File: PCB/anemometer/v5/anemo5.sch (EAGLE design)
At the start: 64 parts, among them IC1 AD8223, IC2 AD8223, IC3 AD8223, IC4 AD8223, IC6 TL072D, J1 RJ12STRAIGHT-I2C, J2 RJ12STRAIGHT-I2C, T1 BC846, T2 BC846, T3 BC846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

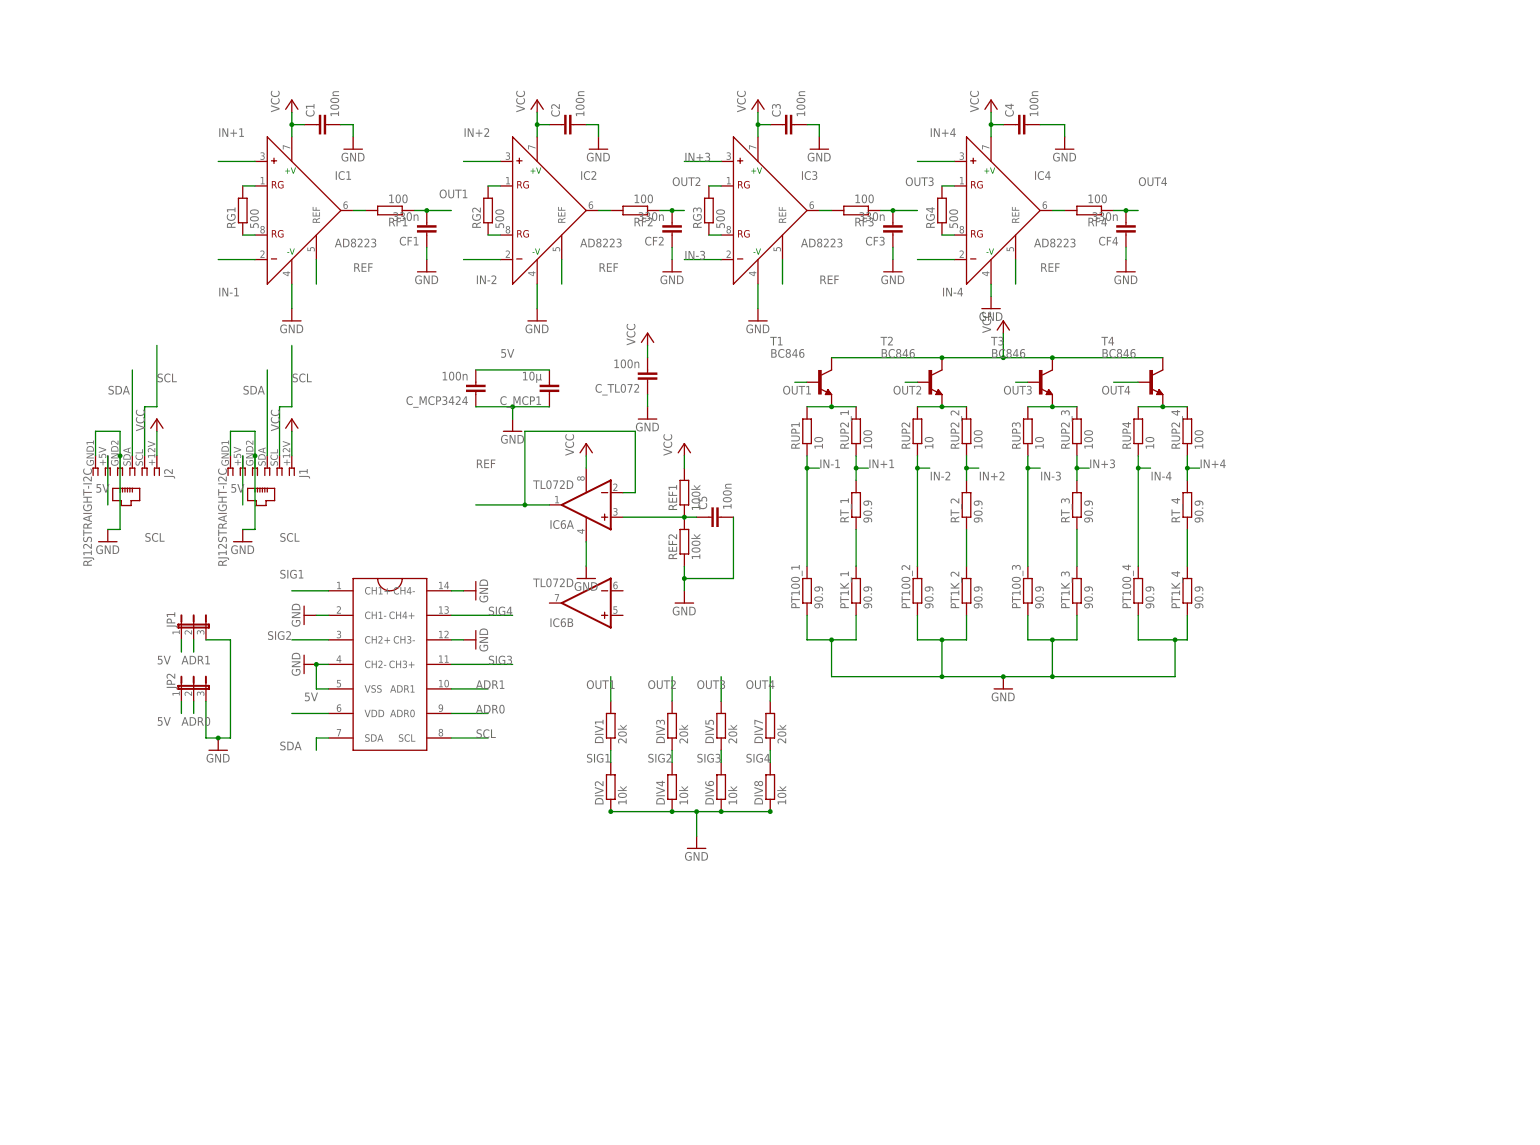
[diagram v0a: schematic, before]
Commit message: created v5 anemometer with identic channels
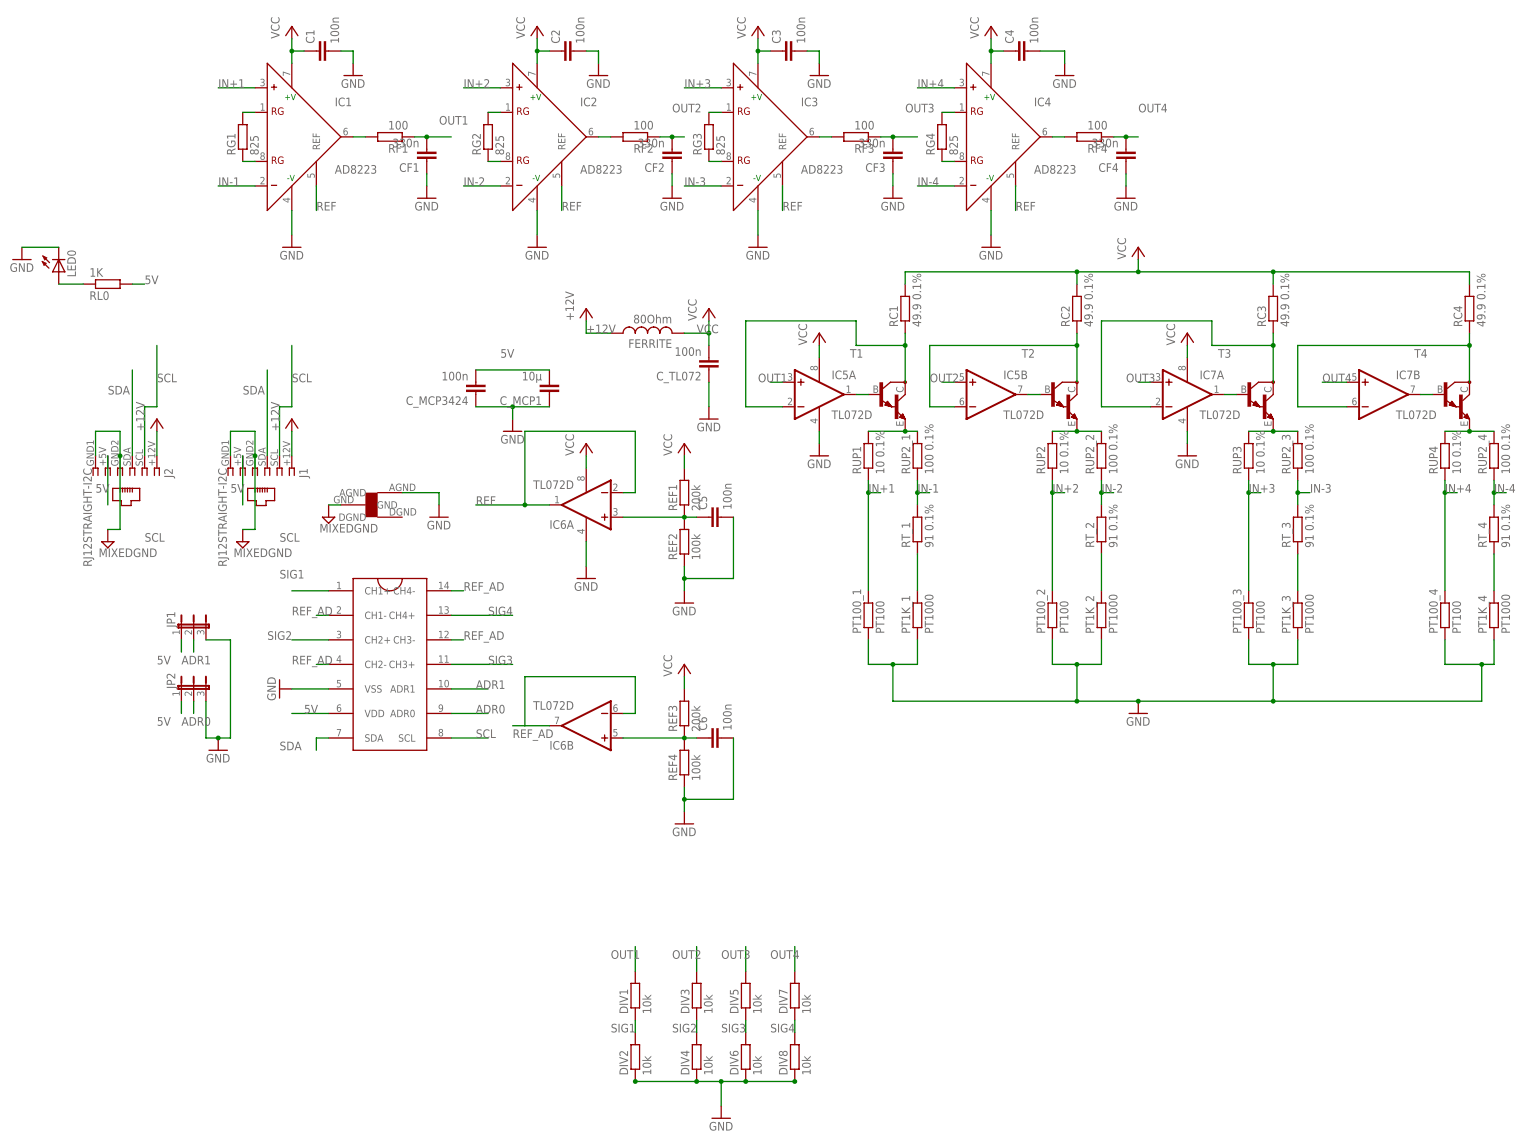
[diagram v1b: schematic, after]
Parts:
- added C6: 100n, rcl:C-EUC1206
- added FERRITE: 80Ohm, rcl:L-USL3216C
- added IC5, IC7: TL072D, linear:TL072D
- added LED0: (no value), SparkFun:LED1206
- added RC1, RC2, RC3, RC4: 49.9 0.1%, resistor:R-EU_M1206
- added REF3: 200k, resistor:R-EU_M1206
- added REF4: 100k, resistor:R-EU_M1206
- added RL0: 1K, resistor:R-EU_M1206
- added U$2: STARGND, lpatiny:STARGND
- DIV1, DIV3, DIV5, DIV7: value 20k -> 10k
- PT100_1, PT100_2, PT100_3, PT100_4: value 90.9 -> PT100
- PT1K_1, PT1K_2, PT1K_3, PT1K_4: value 90.9 -> PT1000
- REF1: value 100k -> 200k
- RG1, RG2, RG3, RG4: value 500 -> 825
- RT_1, RT_2, RT_3, RT_4: value 90.9 -> 91 0.1%
- RUP1, RUP2, RUP3, RUP4: value 10 -> 10 0.1%
- RUP2_1, RUP2_2, RUP2_3, RUP2_4: value 100 -> 100 0.1%
- T1, T2, T3, T4: value BC846 -> (none); device transistor:BC846 -> transistor:MMBTA13LT1-NPN_DARL-SOT23-BEC
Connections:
- new net +12V: FERRITE.1, J1.1, J2.1
- new net MIXEDGND: J1.4, J1.6, J2.4, J2.6, U$2.GND
- new net N$14: LED0.A, RL0.1
- new net N$15: IC5A.-IN, RC1.1, T1.C
- new net N$16: IC5B.-IN, RC2.1, T2.C
- new net N$17: IC7A.-IN, RC3.1, T3.C
- new net N$22: IC7B.-IN, RC4.1, T4.C
- new net N$24: C6.1, REF3.1, REF4.2
- new net OUT1A: IC5A.OUT, T1.B
- new net OUT2A: IC5B.OUT, T2.B
- new net OUT3A: IC7A.OUT, T3.B
- new net OUT4A: IC7B.OUT, T4.B
- new net REF_AD: IC6B.-IN, IC6B.OUT, U$1.CH1-, U$1.CH2-, U$1.CH3-, U$1.CH4-
- net 5V: now also RL0.2
- net GND: now also C6.2, IC5P.V-, IC7P.V-, LED0.C, REF4.1, U$2.AGND; no longer J1.4, J1.6, J2.4, J2.6, U$1.CH1-, U$1.CH2-, U$1.CH3-, U$1.CH4-
- net IN+1: now also PT100_1.2, RUP1.1; no longer RT_1.2, RUP2_1.1
- net IN+2: now also PT100_2.2, RUP2.1; no longer RT_2.2, RUP2_2.1
- net IN+3: now also PT100_3.2, RUP3.1; no longer RT_3.2, RUP2_3.1
- net IN+4: now also PT100_4.2, RUP4.1; no longer RT_4.2, RUP2_4.1
- net IN-1: now also RT_1.2, RUP2_1.1; no longer PT100_1.2, RUP1.1
- net IN-2: now also RT_2.2, RUP2_2.1; no longer PT100_2.2, RUP2.1
- net IN-3: now also RT_3.2, RUP2_3.1; no longer PT100_3.2, RUP3.1
- net IN-4: now also RT_4.2, RUP2_4.1; no longer PT100_4.2, RUP4.1
- net OUT1: now also IC5A.+IN; no longer T1.B
- net OUT2: now also IC5B.+IN; no longer T2.B
- net OUT3: now also IC7A.+IN; no longer T3.B
- net OUT4: now also IC7B.+IN; no longer T4.B
- net VCC: now also FERRITE.2, IC5P.V+, IC7P.V+, RC1.2, RC2.2, RC3.2, RC4.2, REF3.2; no longer J1.1, J2.1, T1.C, T2.C, T3.C, T4.C
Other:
- moved on the sheet: C1, C2, C3, C4, CF1, CF2, CF3, CF4, C_TL072, DIV1, DIV2, DIV3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
